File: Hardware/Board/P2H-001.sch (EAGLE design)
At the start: 15 parts, among them IC1 74LS07N, IC2 LTC485N

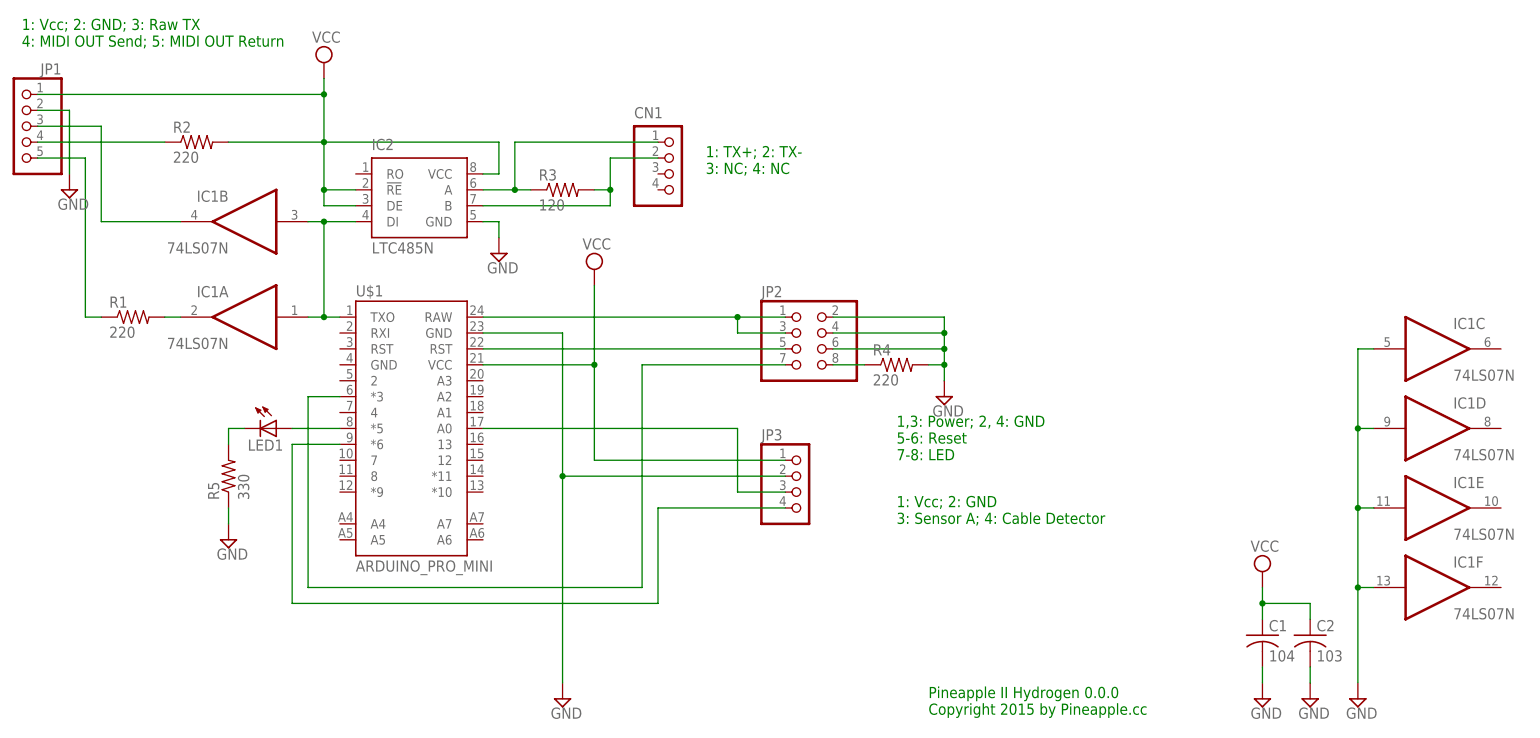
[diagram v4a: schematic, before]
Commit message: Adopted to the new pinout.
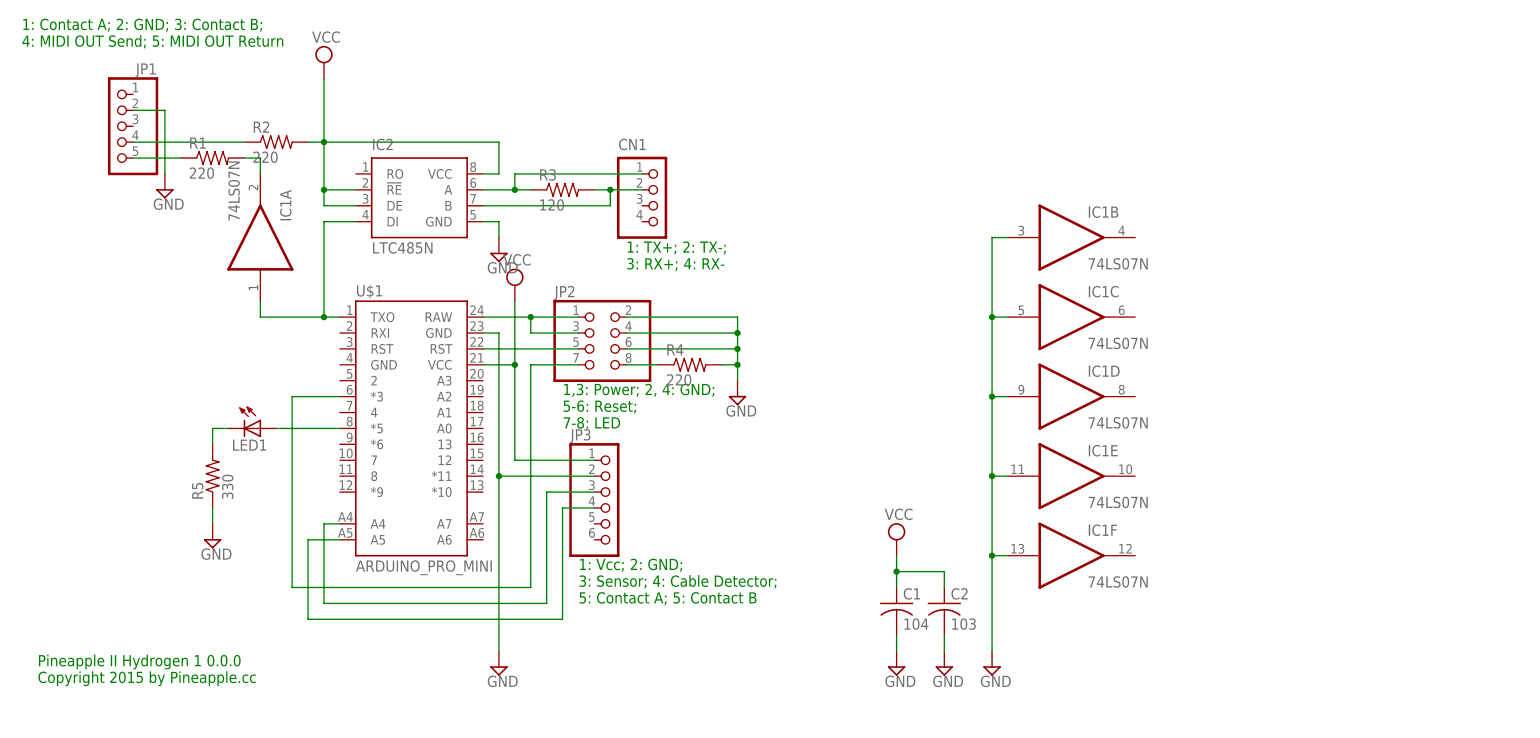
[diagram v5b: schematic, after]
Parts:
- JP3: device pinhead:PINHD-1X4 -> pinhead:PINHD-1X6
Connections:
- removed net N$4: IC1B.O, JP1.3
- net GND: now also IC1B.I
- net N$1: no longer IC1B.I
- net N$10: now also U$1.A4; no longer U$1.A0
- net N$11: now also U$1.A5; no longer U$1.*6
- net VCC: no longer JP1.1
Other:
- note added: "1,3: Power; 2, 4: GND; 5-6: Reset; 7-8: LED"
- note added: "1: Contact A; 2: GND; 3: Contact B; 4: MIDI OUT Send; 5: MIDI OUT Return"
- note added: "1: TX+; 2: TX-; 3: RX+; 4: RX-"
- note added: "1: Vcc; 2: GND; 3: Sensor; 4: Cable Detector; 5: Contact A; 5: Contact B"
- note added: "Pineapple II Hydrogen 1 0.0.0 Copyright 2015 by Pineapple.cc"
- note removed: "1,3: Power; 2, 4: GND 5-6: Reset 7-8: LED"
- note removed: "1: TX+; 2: TX- 3: NC; 4: NC"
- note removed: "1: Vcc; 2: GND 3: Sensor A; 4: Cable Detector"
- note removed: "1: Vcc; 2: GND; 3: Raw TX 4: MIDI OUT Send; 5: MIDI OUT Return"
- note removed: "Pineapple II Hydrogen 0.0.0 Copyright 2015 by Pineapple.cc"
- moved on the sheet: C1, C2, CN1, IC1A, IC1B, IC1C, IC1D, IC1E, IC1F, JP1, JP2, LED1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

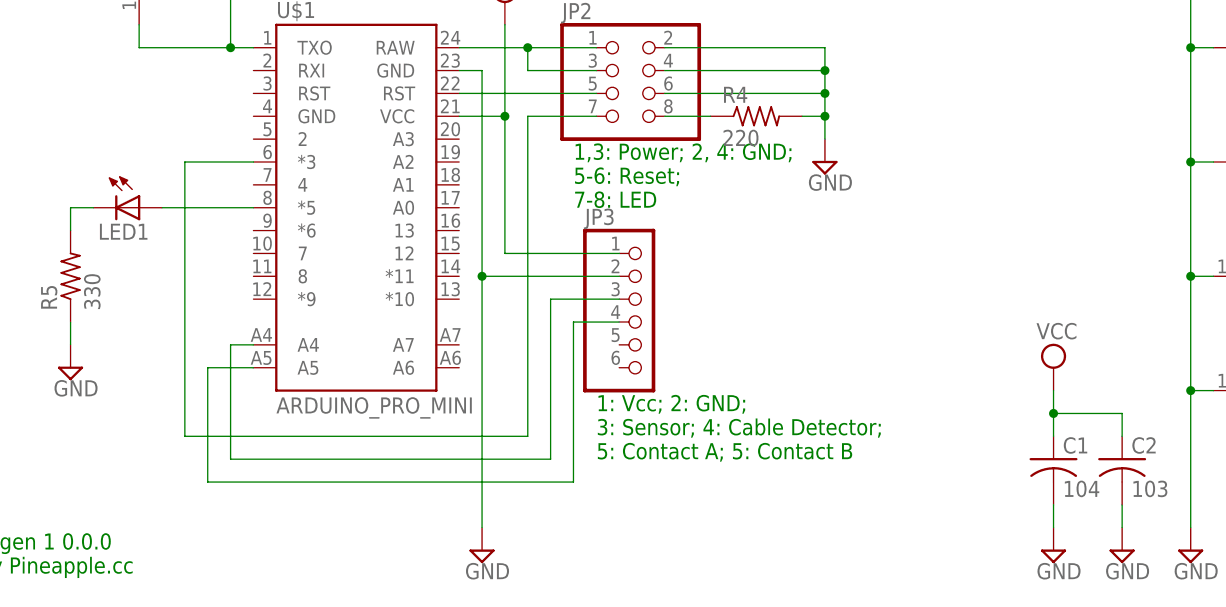
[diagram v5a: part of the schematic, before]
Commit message: Adopted new Hydroport pinout.
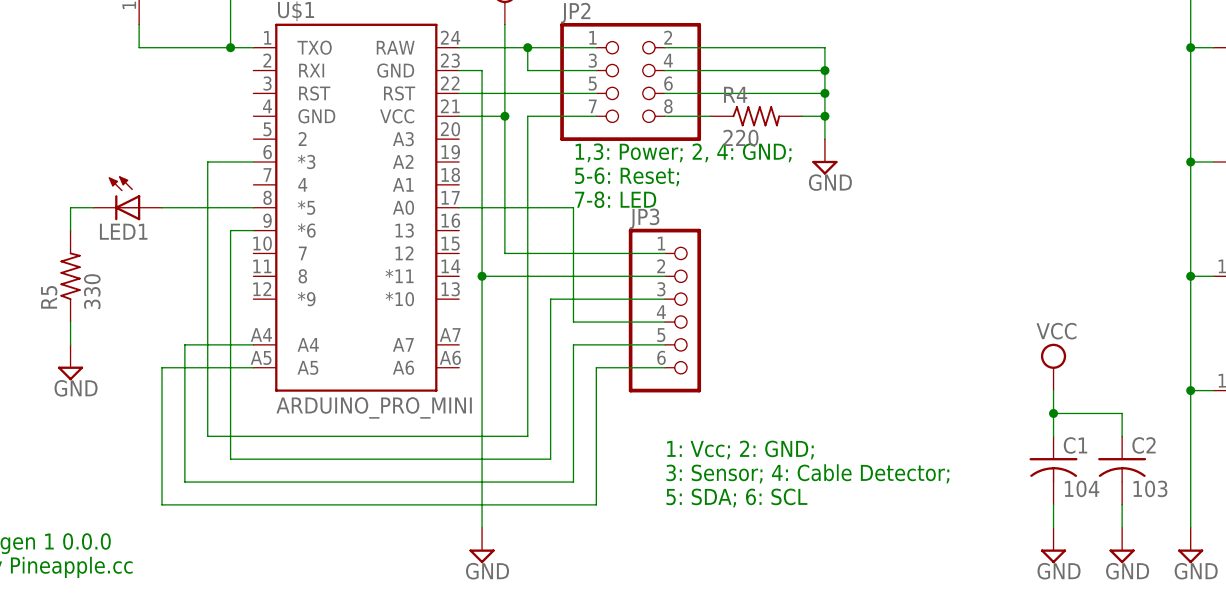
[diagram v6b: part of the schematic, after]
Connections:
- new net N$14: JP3.6, U$1.A5
- new net N$4: JP3.4, U$1.A0
- net N$10: now also U$1.*6; no longer U$1.A4
- net N$11: now also JP3.5, U$1.A4; no longer JP3.4, U$1.A5
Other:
- note added: "1: Vcc; 2: GND; 3: Sensor; 4: Cable Detector; 5: SDA; 6: SCL"
- note removed: "1: Vcc; 2: GND; 3: Sensor; 4: Cable Detector; 5: Contact A; 5: Contact B"
- moved on the sheet: JP3
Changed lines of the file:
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@@
 5-6: Reset;
 7-8: LED</text>
-<text x="99.06" y="0" size="1.778" layer="91">1: Vcc; 2: GND;
+<text x="106.68" y="-5.08" size="1.778" layer="91">1: Vcc; 2: GND;
 3: Sensor; 4: Cable Detector;
-5: Contact A; 5: Contact B</text>
+5: SDA; 6: SCL</text>
 </plain>
 <instances>
@@
 <instance part="SUPPLY6" gate="GND" x="124.46" y="33.02"/>
 <instance part="R4" gate="G$1" x="116.84" y="38.1"/>
-<instance part="JP3" gate="A" x="104.14" y="15.24"/>
+<instance part="JP3" gate="A" x="109.22" y="15.24"/>
 <instance part="IC2" gate="G$1" x="73.66" y="66.04"/>
 <instance part="R3" gate="G$1" x="96.52" y="66.04"/>
@@
 <pinref part="JP3" gate="A" pin="2"/>
 <wire x1="86.36" y1="20.32" x2="86.36" y2="-7.62" width="0.1524" layer="91"/>
-<wire x1="101.6" y1="20.32" x2="86.36" y2="20.32" width="0.1524" layer="91"/>
+<wire x1="106.68" y1="20.32" x2="86.36" y2="20.32" width="0.1524" layer="91"/>
 <junction x="86.36" y="20.32"/>
 <pinref part="U$1" gate="G$1" pin="GND@2"/>
@@
 <wire x1="88.9" y1="38.1" x2="88.9" y2="22.86" width="0.1524" layer="91"/>
 <pinref part="JP3" gate="A" pin="1"/>
-<wire x1="88.9" y1="22.86" x2="101.6" y2="22.86" width="0.1524" layer="91"/>
+<wire x1="88.9" y1="22.86" x2="106.68" y2="22.86" width="0.1524" layer="91"/>
 <junction x="88.9" y="38.1"/>
 <pinref part="U$1" gate="G$1" pin="VCC"/>
@@
 <net name="N$8" class="0">
 <segment>
-<wire x1="60.96" y1="33.02" x2="53.34" y2="33.02" width="0.1524" layer="91"/>
-<wire x1="53.34" y1="33.02" x2="53.34" y2="2.54" width="0.1524" layer="91"/>
-<wire x1="53.34" y1="2.54" x2="91.44" y2="2.54" width="0.1524" layer="91"/>
+<wire x1="60.96" y1="33.02" x2="55.88" y2="33.02" width="0.1524" layer="91"/>
+<wire x1="55.88" y1="33.02" x2="55.88" y2="2.54" width="0.1524" layer="91"/>
+<wire x1="55.88" y1="2.54" x2="91.44" y2="2.54" width="0.1524" layer="91"/>
 <wire x1="91.44" y1="2.54" x2="91.44" y2="38.1" width="0.1524" layer="91"/>
 <pinref part="JP2" gate="A" pin="7"/>
@@
 </segment>
 </net>
-<net name="N$10" class="0">
-<segment>
-<pinref part="JP3" gate="A" pin="3"/>
-<wire x1="101.6" y1="17.78" x2="93.98" y2="17.78" width="0.1524" layer="91"/>
-<wire x1="93.98" y1="17.78" x2="93.98" y2="0" width="0.1524" layer="91"/>
-<wire x1="93.98" y1="0" x2="58.42" y2="0" width="0.1524" layer="91"/>
-<wire x1="58.42" y1="0" x2="58.42" y2="12.7" width="0.1524" layer="91"/>
-<pinref part="U$1" gate="G$1" pin="A4"/>
-<wire x1="58.42" y1="12.7" x2="60.96" y2="12.7" width="0.1524" layer="91"/>
-</segment>
-</net>
-<net name="N$11" class="0">
-<segment>
-<pinref part="U$1" gate="G$1" pin="A5"/>
-<wire x1="60.96" y1="10.16" x2="55.88" y2="10.16" width="0.1524" layer="91"/>
-<wire x1="55.88" y1="10.16" x2="55.88" y2="-2.54" width="0.1524" layer="91"/>
-<wire x1="55.88" y1="-2.54" x2="96.52" y2="-2.54" width="0.1524" layer="91"/>
-<wire x1="96.52" y1="-2.54" x2="96.52" y2="15.24" width="0.1524" layer="91"/>
-<pinref part="JP3" gate="A" pin="4"/>
-<wire x1="96.52" y1="15.24" x2="101.6" y2="15.24" width="0.1524" layer="91"/>
-</segment>
-</net>
 <net name="N$2" class="0">
 <segment>
@@
 </segment>
 </net>
+<net name="N$4" class="0">
+<segment>
+<pinref part="U$1" gate="G$1" pin="A0"/>
+<wire x1="83.82" y1="27.94" x2="96.52" y2="27.94" width="0.1524" layer="91"/>
+<wire x1="96.52" y1="27.94" x2="96.52" y2="15.24" width="0.1524" layer="91"/>
+<pinref part="JP3" gate="A" pin="4"/>
+<wire x1="96.52" y1="15.24" x2="106.68" y2="15.24" width="0.1524" layer="91"/>
+</segment>
+</net>
+<net name="N$10" class="0">
+<segment>
+<pinref part="U$1" gate="G$1" pin="*6"/>
+<wire x1="60.96" y1="25.4" x2="58.42" y2="25.4" width="0.1524" layer="91"/>
+<wire x1="58.42" y1="25.4" x2="58.42" y2="0" width="0.1524" layer="91"/>
+<wire x1="58.42" y1="0" x2="93.98" y2="0" width="0.1524" layer="91"/>
+<wire x1="93.98" y1="0" x2="93.98" y2="17.78" width="0.1524" layer="91"/>
+<pinref part="JP3" gate="A" pin="3"/>
+<wire x1="106.68" y1="17.78" x2="93.98" y2="17.78" width="0.1524" layer="91"/>
+</segment>
+</net>
+<net name="N$11" class="0">
+<segment>
+<pinref part="U$1" gate="G$1" pin="A4"/>
+<wire x1="60.96" y1="12.7" x2="53.34" y2="12.7" width="0.1524" layer="91"/>
+<wire x1="53.34" y1="12.7" x2="53.34" y2="-2.54" width="0.1524" layer="91"/>
+<wire x1="53.34" y1="-2.54" x2="96.52" y2="-2.54" width="0.1524" layer="91"/>
+<wire x1="96.52" y1="-2.54" x2="96.52" y2="12.7" width="0.1524" layer="91"/>
+<pinref part="JP3" gate="A" pin="5"/>
+<wire x1="96.52" y1="12.7" x2="106.68" y2="12.7" width="0.1524" layer="91"/>
+</segment>
+</net>
+<net name="N$14" class="0">
+<segment>
+<pinref part="U$1" gate="G$1" pin="A5"/>
+<wire x1="60.96" y1="10.16" x2="50.8" y2="10.16" width="0.1524" layer="91"/>
+<wire x1="50.8" y1="10.16" x2="50.8" y2="-5.08" width="0.1524" layer="91"/>
+<wire x1="50.8" y1="-5.08" x2="99.06" y2="-5.08" width="0.1524" layer="91"/>
+<wire x1="99.06" y1="-5.08" x2="99.06" y2="10.16" width="0.1524" layer="91"/>
+<pinref part="JP3" gate="A" pin="6"/>
+<wire x1="99.06" y1="10.16" x2="106.68" y2="10.16" width="0.1524" layer="91"/>
+</segment>
+</net>

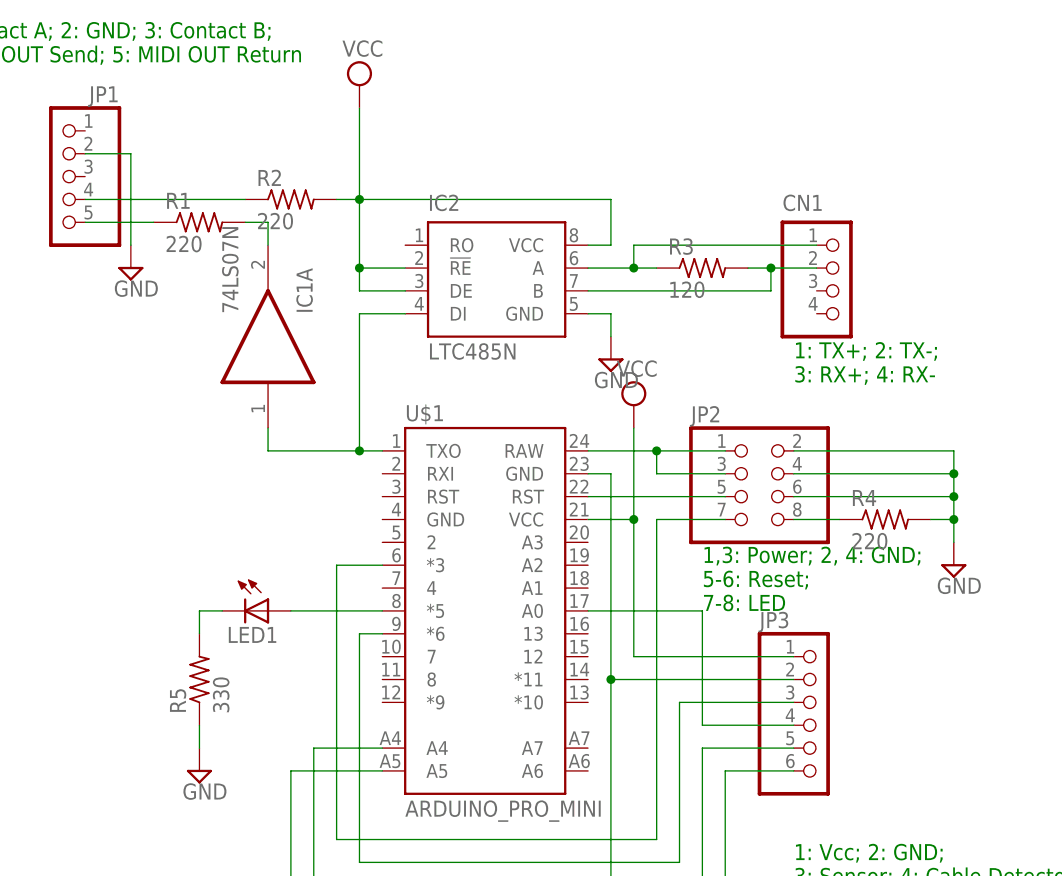
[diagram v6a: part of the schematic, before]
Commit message: Changed layout of ZeroVoltage.
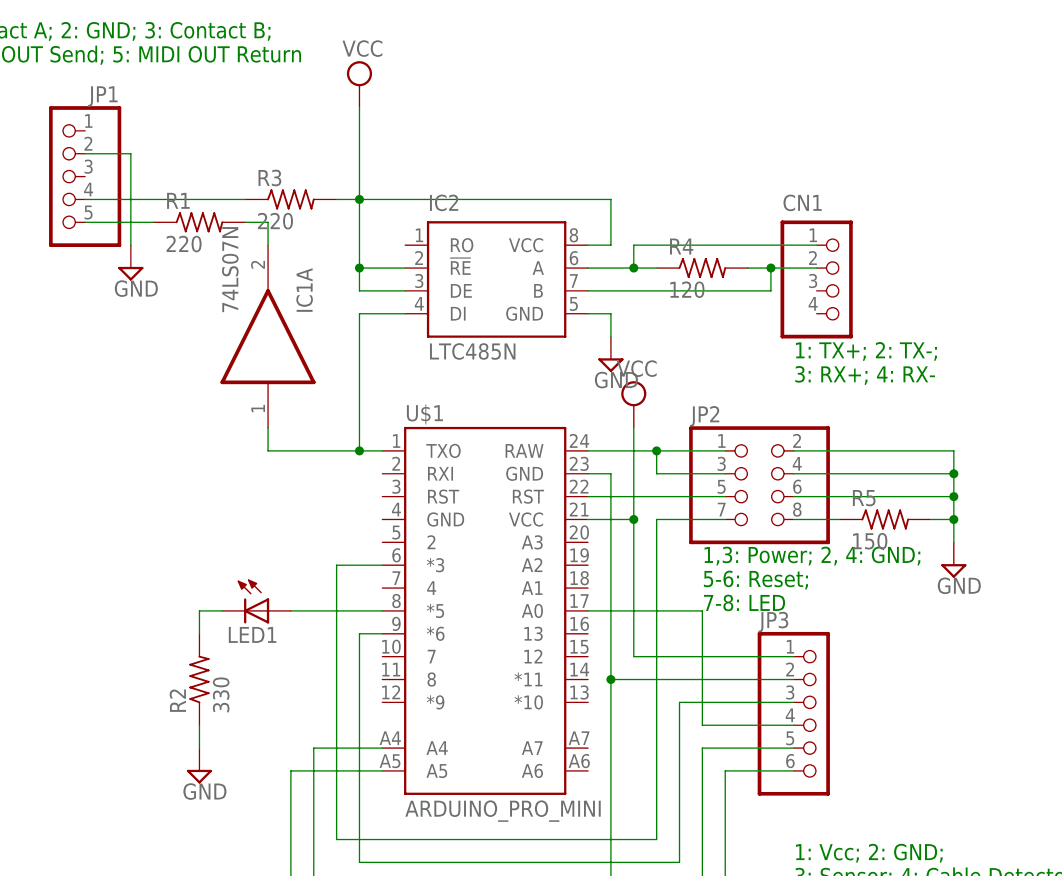
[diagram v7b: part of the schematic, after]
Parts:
- R2: value 220 -> 330
- R3: value 120 -> 220
- R4: value 220 -> 120
- R5: value 330 -> 150
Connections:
- net GND: now also R2.1, R5.2; no longer R4.2, R5.1
- net N$13: now also R2.2; no longer R5.2
- net N$18: now also R4.1; no longer R3.1
- net N$19: now also R4.2; no longer R3.2
- net N$3: now also R3.1; no longer R2.1
- net N$5: now also R5.1; no longer R4.1
- net VCC: now also R3.2; no longer R2.2
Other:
- moved on the sheet: R2, R3, R4, R5

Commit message: Overhaul.
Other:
- note added: "GEEKPORT I (gamma) 1: Vcc; 2: GND; 3: Sensor; 4: Cable Detector; 5: SDA; 6: SCL"
- note added: "HYDROGEN CONNECTOR (h) 1,3: Power; 2, 4: GND; 5-6: Reset; 7-8: LED"
- note added: "MIDIOUT (m0) 1: NC; 2: GND; 3: NC; 4: MIDI OUT Send; 5: MIDI OUT Return"
- note added: "MIDISTANCE (c) 1: TX+; 2: TX-; 3: NC; 4: NC"
- note added: "Pineapple II Hydrogen 1.0.0 Copyright 2015 by Pineapple.cc"
- note removed: "1,3: Power; 2, 4: GND; 5-6: Reset; 7-8: LED"
- note removed: "1: Contact A; 2: GND; 3: Contact B; 4: MIDI OUT Send; 5: MIDI OUT Return"
- note removed: "1: TX+; 2: TX-; 3: RX+; 4: RX-"
- note removed: "1: Vcc; 2: GND; 3: Sensor; 4: Cable Detector; 5: SDA; 6: SCL"
- note removed: "Pineapple II Hydrogen 1 0.0.0 Copyright 2015 by Pineapple.cc"
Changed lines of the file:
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@@
 <sheet>
 <plain>
-<text x="12.7" y="-12.7" size="1.778" layer="91">Pineapple II Hydrogen 1 0.0.0
+<text x="12.7" y="-12.7" size="1.778" layer="91">Pineapple II Hydrogen 1.0.0
 Copyright 2015 by Pineapple.cc</text>
-<text x="106.68" y="53.34" size="1.778" layer="91">1: TX+; 2: TX-;
-3: RX+; 4: RX-</text>
-<text x="10.16" y="88.9" size="1.778" layer="91">1: Contact A; 2: GND; 3: Contact B;
+<text x="116.84" y="63.5" size="1.778" layer="91">MIDISTANCE (c)
+1: TX+; 2: TX-;
+3: NC; 4: NC</text>
+<text x="10.16" y="86.36" size="1.778" layer="91">MIDIOUT (m0)
+1: NC; 2: GND; 3: NC;
 4: MIDI OUT Send; 5: MIDI OUT Return</text>
-<text x="96.52" y="27.94" size="1.778" layer="91">1,3: Power; 2, 4: GND;
+<text x="127" y="40.64" size="1.778" layer="91">HYDROGEN CONNECTOR (h)
+1,3: Power; 2, 4: GND;
 5-6: Reset;
 7-8: LED</text>
-<text x="106.68" y="-5.08" size="1.778" layer="91">1: Vcc; 2: GND;
+<text x="106.68" y="-5.08" size="1.778" layer="91">GEEKPORT I (gamma)
+1: Vcc; 2: GND;
 3: Sensor; 4: Cable Detector;
 5: SDA; 6: SCL</text>
